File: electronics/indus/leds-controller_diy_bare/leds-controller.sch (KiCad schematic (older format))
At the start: 10 parts

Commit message: wip bare diy controller - dcdc and refactor
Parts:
- added C1: 10nF, Capacitors_SMD:C_1206, symbol C-RESCUE-leds-controller
- added D1: RS1B DIODE, ab2tech:AB2_DO-214AC, symbol DIODE
- added D2: SM6T68A ou SM36T1G, risebox:DIODE_DO_214_AA, symbol ZENER-RESCUE-leds-controller
- added P2: CONN_01X06, symbol CONN_01X08
- P1: renamed from P?; value ALIM_24V -> ALIM_12V_60V
- gave numbers to parts that had none: 9
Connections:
- net labels added: PWM_COL1, PWM_COL2
- net labels removed: +24V, PWM_BLUE, PWM_RED
- wire segments 63 -> 83
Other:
- moved on the sheet: P1, P3

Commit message: schema done - misses values
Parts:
- removed R1: 10K, symbol R-RESCUE-leds-controller
- removed TH1: THERM CTN 10K, symbol THERMISTOR
- added P?: THERM_LEDS, symbol CONN_01X03
- P2: value CONN_01X06 -> MICRO_CTRL; symbol CONN_01X08 -> CONN_01X10
- P3: value CONN_01X02 -> FANS
- P4: value POT_COLOR1 -> POT_COLOR2
- P5: value POT_COLOR1 -> POT_COLOR3
- P6: value POT_COLOR1 -> POT_COLOR4
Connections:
- net labels added: +12V, +5V, ALIM_LEDS, THERM_CTRL, THERM_LEDS, THERM_OFF
- net labels removed: ALIM_24V, THERM
- wire segments 83 -> 104
- no-connect marks 0 -> 1
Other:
- moved on the sheet: P3, P4, P5, P6, P7, P8, P9

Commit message: schema prctically ok missing refs
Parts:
- added R? (x5): 1k, symbol R
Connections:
- net GND: now also P2.10 (P10)
- net PWM_COL1: now also R?.1; no longer P2.6 (P6)
- net PWM_COL2: now also R?.1; no longer P2.5 (P5)
- net PWM_COL3: now also R?.1; no longer P2.4 (P4)
- net PWM_COL4: now also R?.1; no longer P2.3 (P3)
- net PWM_FANS: now also R?.1; no longer P2.2 (P2)
- new net: P2.2 (P2), R?.2
- new net: P2.3 (P3), R?.2
- new net: P2.4 (P4), R?.2
- new net: P2.5 (P5), R?.2
- new net: P2.6 (P6), R?.2
- no-connect marks 1 -> 0
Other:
- note added: "Chaque potard permet de dimer analogiquement\nen réduisant linéairement la tension appliquée sur\nla PIN IADJ de chaque controlleur."
- note added: "SECURITE THERMIQUE\n- les controlleurs s'arrètent à une certaine T°\n- la T° des cartes de leds est prise en compte aussi"
- moved on the sheet: P2, P?

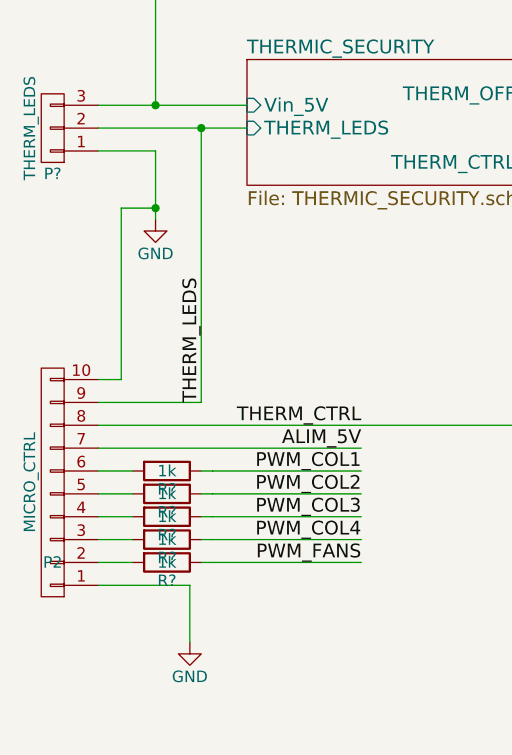
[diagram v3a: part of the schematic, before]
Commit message: schema prctically ok missing refs
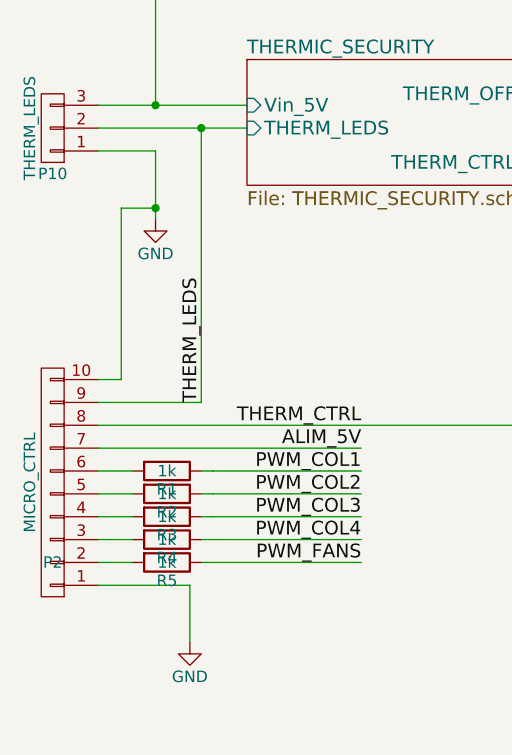
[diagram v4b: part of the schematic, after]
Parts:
- gave numbers to parts that had none: 6
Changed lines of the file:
@@
 $EndComp
 $Comp
-L GND #PWR02
+L GND #PWR9
 U 1 1 576117B3
 P 7050 2150
-F 0 "#PWR02" H 7050 1900 50  0001 C CNN
+F 0 "#PWR9" H 7050 1900 50  0001 C CNN
 F 1 "GND" H 7050 2000 50  0000 C CNN
 F 2 "" H 7050 2150 50  0000 C CNN
@@
 $EndComp
 $Comp
-L GND #PWR03
+L GND #PWR6
 U 1 1 57617728
 P 7000 3350
-F 0 "#PWR03" H 7000 3100 50  0001 C CNN
+F 0 "#PWR6" H 7000 3100 50  0001 C CNN
 F 1 "GND" H 7000 3200 50  0000 C CNN
 F 2 "" H 7000 3350 50  0000 C CNN
@@
 $EndComp
 $Comp
-L GND #PWR04
+L GND #PWR7
 U 1 1 576178E7
 P 7000 4550
-F 0 "#PWR04" H 7000 4300 50  0001 C CNN
+F 0 "#PWR7" H 7000 4300 50  0001 C CNN
 F 1 "GND" H 7000 4400 50  0000 C CNN
 F 2 "" H 7000 4550 50  0000 C CNN
@@
 $EndComp
 $Comp
-L GND #PWR05
+L GND #PWR8
 U 1 1 57617AAD
 P 7000 5750
-F 0 "#PWR05" H 7000 5500 50  0001 C CNN
+F 0 "#PWR8" H 7000 5500 50  0001 C CNN
 F 1 "GND" H 7000 5600 50  0000 C CNN
 F 2 "" H 7000 5750 50  0000 C CNN
@@
 $EndComp
 $Comp
-L GND-RESCUE-leds-controller #PWR07
+L GND-RESCUE-leds-controller #PWR3
 U 1 1 5761ABF9
 P 2050 1900
-F 0 "#PWR07" H 2050 1900 30  0001 C CNN
+F 0 "#PWR3" H 2050 1900 30  0001 C CNN
 F 1 "GND" H 2050 1830 30  0001 C CNN
 F 2 "" H 2050 1900 60  0000 C CNN
@@
 $EndComp
 $Comp
-L GND #PWR08
+L GND #PWR2
 U 1 1 5761F7A3
 P 1450 6000
-F 0 "#PWR08" H 1450 5750 50  0001 C CNN
+F 0 "#PWR2" H 1450 5750 50  0001 C CNN
 F 1 "GND" H 1450 5850 50  0000 C CNN
 F 2 "" H 1450 6000 50  0000 C CNN
@@
 $EndSheet
 $Comp
-L CONN_01X03 P?
+L CONN_01X03 P10
 U 1 1 57631AFC
 P 850 3750
-F 0 "P?" H 850 3950 50  0000 C CNN
+F 0 "P10" H 850 3950 50  0000 C CNN
 F 1 "THERM_LEDS" V 950 3750 50  0000 C CNN
 F 2 "" H 850 3750 50  0000 C CNN
@@
 $EndComp
 $Comp
-L GND #PWR?
+L GND #PWR1
 U 1 1 57631C39
 P 1300 4150
-F 0 "#PWR?" H 1300 3900 50  0001 C CNN
+F 0 "#PWR1" H 1300 3900 50  0001 C CNN
 F 1 "GND" H 1300 4000 50  0000 C CNN
 F 2 "" H 1300 4150 50  0000 C CNN
@@
 PWM_COL4
 $Comp
-L +12V #PWR?
+L +12V #PWR5
 U 1 1 576500F1
 P 5850 1100
-F 0 "#PWR?" H 5850 950 50  0001 C CNN
+F 0 "#PWR5" H 5850 950 50  0001 C CNN
 F 1 "+12V" H 5850 1240 50  0000 C CNN
 F 2 "" H 5850 1100 50  0000 C CNN
@@
 $EndComp
 $Comp
-L +5V #PWR?
+L +5V #PWR4
 U 1 1 57655059
 P 5850 800
-F 0 "#PWR?" H 5850 650 50  0001 C CNN
+F 0 "#PWR4" H 5850 650 50  0001 C CNN
 F 1 "+5V" H 5850 940 50  0000 C CNN
 F 2 "" H 5850 800 50  0000 C CNN
@@
 $EndComp
 $Comp
-L +12V #PWR?
+L +12V #PWR10
 U 1 1 57656258
 P 8750 5650
-F 0 "#PWR?" H 8750 5500 50  0001 C CNN
+F 0 "#PWR10" H 8750 5500 50  0001 C CNN
 F 1 "+12V" H 8750 5790 50  0000 C CNN
 F 2 "" H 8750 5650 50  0000 C CNN
@@
 	1050 4850 1150 4850
 $Comp
-L R R?
+L R R1
 U 1 1 5764FDF1
 P 1350 5250
-F 0 "R?" V 1430 5250 50  0000 C CNN
+F 0 "R1" V 1430 5250 50  0000 C CNN
 F 1 "1k" V 1350 5250 50  0000 C CNN
 F 2 "" V 1280 5250 50  0000 C CNN
@@
 	1200 5350 1050 5350
 $Comp
-L R R?
+L R R2
 U 1 1 5765059C
 P 1350 5350
-F 0 "R?" V 1430 5350 50  0000 C CNN
+F 0 "R2" V 1430 5350 50  0000 C CNN
 F 1 "1k" V 1350 5350 50  0000 C CNN
 F 2 "" V 1280 5350 50  0000 C CNN
@@
 	1200 5450 1050 5450
 $Comp
-L R R?
+L R R3
 U 1 1 57650987
 P 1350 5450
-F 0 "R?" V 1430 5450 50  0000 C CNN
+F 0 "R3" V 1430 5450 50  0000 C CNN
 F 1 "1k" V 1350 5450 50  0000 C CNN
 F 2 "" V 1280 5450 50  0000 C CNN
@@
 	1200 5550 1050 5550
 $Comp
-L R R?
+L R R4
 U 1 1 57650B23
 P 1350 5550
-F 0 "R?" V 1430 5550 50  0000 C CNN
+F 0 "R4" V 1430 5550 50  0000 C CNN
 F 1 "1k" V 1350 5550 50  0000 C CNN
 F 2 "" V 1280 5550 50  0000 C CNN
@@
 	1200 5650 1050 5650
 $Comp
-L R R?
+L R R5
 U 1 1 57650CC5
 P 1350 5650
-F 0 "R?" V 1430 5650 50  0000 C CNN
+F 0 "R5" V 1430 5650 50  0000 C CNN
 F 1 "1k" V 1350 5650 50  0000 C CNN
 F 2 "" V 1280 5650 50  0000 C CNN

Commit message: bom refs etc
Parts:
- D2: value SM6T68A ou SM36T1G -> SMAJ54A
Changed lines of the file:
@@
 P 2050 1350
 F 0 "D2" H 2050 1450 50  0000 C CNN
-F 1 "SM6T68A ou SM36T1G" H 2050 1250 40  0000 C CNN
+F 1 "SMAJ54A" H 2050 1250 40  0000 C CNN
 F 2 "risebox:DIODE_DO_214_AA" H 2050 1350 60  0001 C CNN
 F 3 "" H 2050 1350 60  0000 C CNN

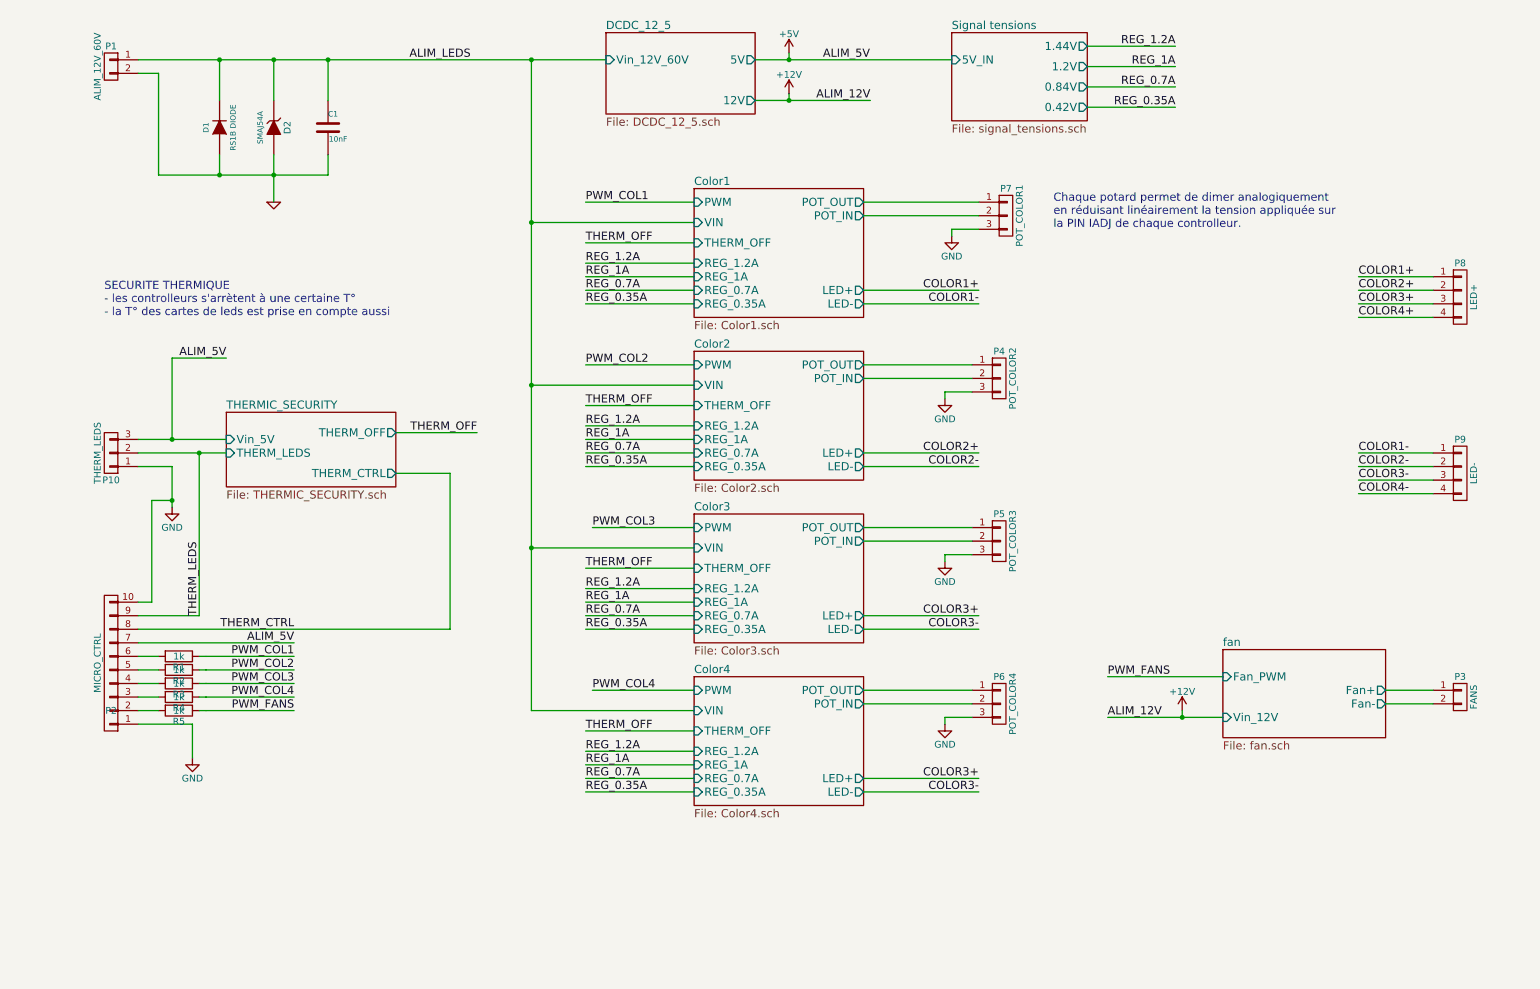
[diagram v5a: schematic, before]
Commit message: simpler schematics with a lot of values now
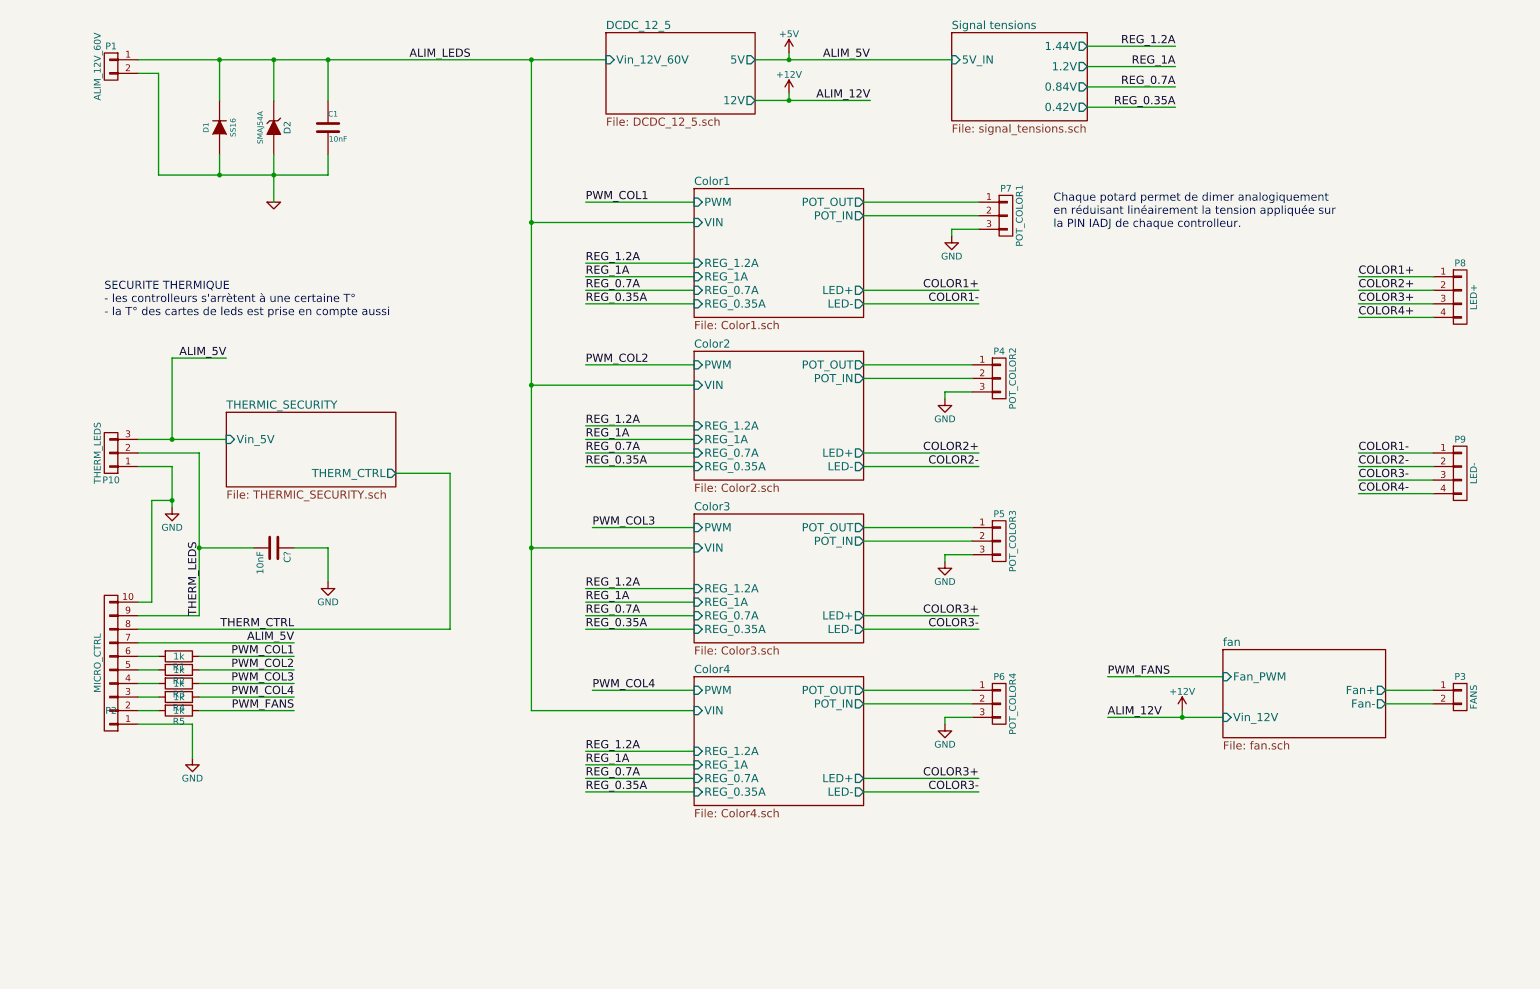
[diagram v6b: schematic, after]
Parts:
- added C?: 10nF, symbol C
- D1: value RS1B DIODE -> SS16
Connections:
- net GND: now also C?.1
- net THERM_LEDS: now also C?.2
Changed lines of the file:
@@
 F10 "POT_IN" O R 6400 3200 60
 F11 "POT_OUT" O R 6400 3100 60
-F12 "THERM_OFF" I L 5150 3400 60
 $EndSheet
 $Sheet
@@
 F10 "POT_IN" O R 6400 2000 60
 F11 "POT_OUT" O R 6400 1900 60
-F12 "THERM_OFF" I L 5150 2200 60
 $EndSheet
 $Sheet
@@
 F10 "POT_IN" O R 6400 4400 60
 F11 "POT_OUT" O R 6400 4300 60
-F12 "THERM_OFF" I L 5150 4600 60
 $EndSheet
 $Sheet
@@
 F10 "POT_IN" O R 6400 5600 60
 F11 "POT_OUT" O R 6400 5500 60
-F12 "THERM_OFF" I L 5150 5800 60
 $EndSheet
 $Comp
@@
 P 1650 1350
 F 0 "D1" H 1650 1450 40  0000 C CNN
-F 1 "RS1B DIODE" H 1650 1250 40  0000 C CNN
+F 1 "SS16" H 1650 1250 40  0000 C CNN
 F 2 "ab2tech:AB2_DO-214AC" H 1650 1350 60  0001 C CNN
 F 3 "" H 1650 1350 60  0000 C CNN
@@
 F1 "THERMIC_SECURITY.sch" 60
 F2 "Vin_5V" I L 1700 3650 60
-F3 "THERM_OFF" O R 2950 3600 60
-F4 "THERM_LEDS" I L 1700 3750 60
-F5 "THERM_CTRL" O R 2950 3900 60
+F3 "THERM_CTRL" O R 2950 3900 60
 $EndSheet
 $Comp
@@
 	1    0    0    -1
 $EndComp
-Text Label 4350 2200 0    60   ~ 0
-THERM_OFF
-Text Label 3550 3600 2    60   ~ 0
-THERM_OFF
 Text Label 2200 5250 2    60   ~ 0
 PWM_COL1
@@
 Text Label 4350 3850 0    60   ~ 0
 REG_0.35A
-Text Label 4350 3400 0    60   ~ 0
-THERM_OFF
 Text Label 3050 850  0    60   ~ 0
 ALIM_LEDS
@@
 	5150 1900 4350 1900
 Wire Wire Line
-	2950 3600 3550 3600
-Wire Wire Line
-	1050 3650 1300 3650
-Wire Wire Line
-	1300 3650 1700 3650
-Wire Wire Line
-	1700 3750 1500 3750
-Wire Wire Line
-	1500 3750 1050 3750
+	1050 3650 1700 3650
 Wire Wire Line
 	5150 2050 3950 2050
 Connection ~ 3950 850
 Wire Wire Line
-	5150 2200 4350 2200
-Wire Wire Line
-	1300 3850 1300 4100
-Wire Wire Line
-	1300 4100 1300 4150
+	1300 3850 1300 4150
 Wire Wire Line
 	1050 3850 1300 3850
 Wire Wire Line
-	5600 1150 5850 1150
-Wire Wire Line
-	5850 1150 6450 1150
-Wire Wire Line
-	5600 850  5850 850
-Wire Wire Line
-	5850 850  7050 850
+	5600 1150 6450 1150
+Wire Wire Line
+	5600 850  7050 850
 Wire Wire Line
 	1450 5750 1450 6000
@@
 	1650 1550 1650 1700
 Wire Wire Line
-	2050 1550 2050 1700
-Wire Wire Line
-	2050 1700 2050 1900
-Wire Wire Line
-	1200 1700 1650 1700
-Wire Wire Line
-	1650 1700 2050 1700
-Wire Wire Line
-	2050 1700 2450 1700
+	2050 1550 2050 1900
+Wire Wire Line
+	1200 1700 2450 1700
 Connection ~ 2450 850
 Wire Wire Line
@@
 	1050 5150 2200 5150
 Wire Wire Line
-	2200 5250 1550 5250
-Wire Wire Line
-	1550 5250 1500 5250
+	1500 5250 2200 5250
 Wire Wire Line
 	1200 5250 1050 5250
@@
 	3950 5650 5150 5650
 Wire Wire Line
-	3950 850  3950 2050
-Wire Wire Line
-	3950 2050 3950 3250
-Wire Wire Line
-	3950 3250 3950 4450
-Wire Wire Line
-	3950 4450 3950 5650
+	3950 850  3950 5650
 Wire Wire Line
 	10250 5500 10600 5500
@@
 	8200 5400 9050 5400
 Wire Wire Line
-	8200 5700 8750 5700
-Wire Wire Line
-	8750 5700 9050 5700
-Wire Wire Line
-	1050 850  1650 850
-Wire Wire Line
-	1650 850  2050 850
-Wire Wire Line
-	2050 850  2450 850
-Wire Wire Line
-	2450 850  3950 850
-Wire Wire Line
-	3950 850  4500 850
+	8200 5700 9050 5700
+Wire Wire Line
+	1050 850  4500 850
 Wire Wire Line
 	1200 950  1200 1700
@@
 	6400 3750 7250 3750
 Wire Wire Line
-	5150 3400 4350 3400
-Wire Wire Line
 	5150 3850 4350 3850
 Wire Wire Line
@@
 Wire Wire Line
 	1500 4950 1050 4950
-Connection ~ 1500 3750
 Text Label 4350 4750 0    60   ~ 0
 REG_1.2A
@@
 Text Label 4350 5050 0    60   ~ 0
 REG_0.35A
-Text Label 4350 4600 0    60   ~ 0
-THERM_OFF
-Wire Wire Line
-	5150 4600 4350 4600
 Wire Wire Line
 	5150 5050 4350 5050
@@
 Text Label 4350 6250 0    60   ~ 0
 REG_0.35A
-Text Label 4350 5800 0    60   ~ 0
-THERM_OFF
-Wire Wire Line
-	5150 5800 4350 5800
 Wire Wire Line
 	5150 6250 4350 6250
@@
 $EndComp
 Wire Wire Line
-	2200 5350 1550 5350
-Wire Wire Line
-	1550 5350 1500 5350
+	1500 5350 2200 5350
 Wire Wire Line
 	1200 5350 1050 5350
@@
 $EndComp
 Wire Wire Line
-	2200 5450 1550 5450
-Wire Wire Line
-	1550 5450 1500 5450
+	1500 5450 2200 5450
 Wire Wire Line
 	1200 5450 1050 5450
@@
 $EndComp
 Wire Wire Line
-	2200 5550 1550 5550
-Wire Wire Line
-	1550 5550 1500 5550
+	1500 5550 2200 5550
 Wire Wire Line
 	1200 5550 1050 5550
@@
 $EndComp
 Wire Wire Line
-	2200 5650 1550 5650
-Wire Wire Line
-	1550 5650 1500 5650
+	1500 5650 2200 5650
 Wire Wire Line
 	1200 5650 1050 5650
@@
 Text Notes 800  2750 0    60   ~ 0
 SECURITE THERMIQUE\n- les controlleurs s'arrètent à une certaine T°\n- la T° des cartes de leds est prise en compte aussi
+Wire Wire Line
+	1500 4450 1900 4450
+Connection ~ 1500 4450
+$Comp
+L C C?
+U 1 1 57683C7B
+P 2050 4450
+F 0 "C?" H 2075 4550 50  0000 L CNN
+F 1 "10nF" H 2075 4350 50  0000 L CNN
+F 2 "" H 2088 4300 50  0000 C CNN
+F 3 "" H 2050 4450 50  0000 C CNN
+	1    2050 4450
+	0    1    1    0
+$EndComp
+$Comp
+L GND #PWR?
+U 1 1 576840C0
+P 2450 4700
+F 0 "#PWR?" H 2450 4450 50  0001 C CNN
+F 1 "GND" H 2450 4550 50  0000 C CNN
+F 2 "" H 2450 4700 50  0000 C CNN
+F 3 "" H 2450 4700 50  0000 C CNN
+	1    2450 4700
+	1    0    0    -1
+$EndComp
+Wire Wire Line
+	2200 4450 2450 4450
+Wire Wire Line
+	2450 4450 2450 4700
+Wire Wire Line
+	1050 3750 1500 3750
 $EndSCHEMATC

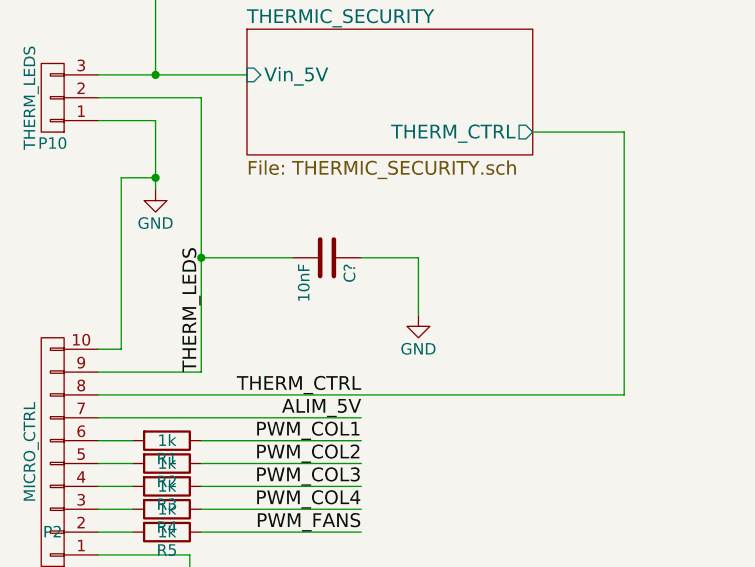
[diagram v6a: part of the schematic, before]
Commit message: Added missing Capa & Resistor values
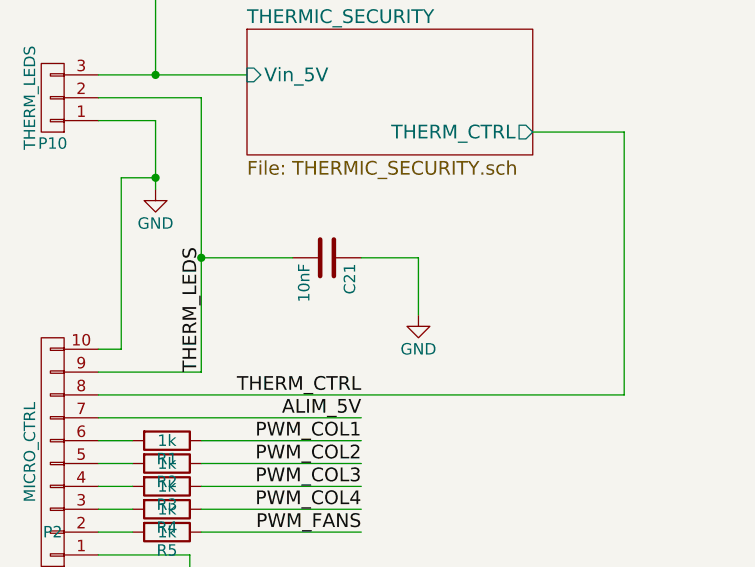
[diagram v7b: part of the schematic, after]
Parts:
- R1, R2: footprint (none) -> Resistors_SMD:R_0805
- gave numbers to parts that had none: 1
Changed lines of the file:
@@
 F 0 "R1" V 1430 5250 50  0000 C CNN
 F 1 "1k" V 1350 5250 50  0000 C CNN
-F 2 "" V 1280 5250 50  0000 C CNN
+F 2 "Resistors_SMD:R_0805" V 1280 5250 50  0001 C CNN
 F 3 "" H 1350 5250 50  0000 C CNN
 	1    1350 5250
@@
 F 0 "R2" V 1430 5350 50  0000 C CNN
 F 1 "1k" V 1350 5350 50  0000 C CNN
-F 2 "" V 1280 5350 50  0000 C CNN
+F 2 "Resistors_SMD:R_0805" V 1280 5350 50  0001 C CNN
 F 3 "" H 1350 5350 50  0000 C CNN
 	1    1350 5350
@@
 Connection ~ 1500 4450
 $Comp
-L C C?
+L C C21
 U 1 1 57683C7B
 P 2050 4450
-F 0 "C?" H 2075 4550 50  0000 L CNN
+F 0 "C21" H 2075 4550 50  0000 L CNN
 F 1 "10nF" H 2075 4350 50  0000 L CNN
 F 2 "" H 2088 4300 50  0000 C CNN
